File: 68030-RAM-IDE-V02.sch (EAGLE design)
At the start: 71 parts, among them IC1 REG1117, IC10 ICS570B, IC2 74HCT245PW, IC3 74AC16245, IC4 AM29F010S, IC5 74ALVT16543, IC6 74ALVT16543, IC7 XC95288XL-TQ144, IC8 K4S56163, IC9 K4S56163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

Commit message: burst still buggy :(
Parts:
- added C37, C38: 100pF, rcl:C-EUC0603K
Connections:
- net GND: now also C37.2, C38.2
- net LE_30_RAM: now also C38.1
- net LE_RAM_30: now also C37.1

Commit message: fooling around mit cl2
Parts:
- R10, R11: value (none) -> 33
- R12, R13: value (none) -> 4k7
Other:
- moved on the sheet: C36, IC10G$2, SJ1
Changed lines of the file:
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@@
 <part name="SJ1" library="jumper" deviceset="SJ2W" device=""/>
 <part name="C36" library="rcl" deviceset="C-EU" device="C0603K"/>
-<part name="R10" library="rcl" deviceset="R-EU_" device="R0603"/>
-<part name="R11" library="rcl" deviceset="R-EU_" device="R0603"/>
-<part name="R12" library="rcl" deviceset="R-EU_" device="R0603"/>
-<part name="R13" library="rcl" deviceset="R-EU_" device="R0603"/>
+<part name="R10" library="rcl" deviceset="R-EU_" device="R0603" value="33"/>
+<part name="R11" library="rcl" deviceset="R-EU_" device="R0603" value="33"/>
+<part name="R12" library="rcl" deviceset="R-EU_" device="R0603" value="4k7"/>
+<part name="R13" library="rcl" deviceset="R-EU_" device="R0603" value="4k7"/>
 <part name="SJ2" library="jumper" deviceset="SJ2W" device=""/>
 <part name="C37" library="rcl" deviceset="C-EU" device="C0603K" value="100pF"/>
@@
 <instance part="GND33" gate="1" x="66.04" y="5.08"/>
 <instance part="IC10" gate="G$1" x="200.66" y="142.24"/>
-<instance part="IC10" gate="G$2" x="215.9" y="116.84"/>
-<instance part="GND34" gate="1" x="215.9" y="104.14"/>
-<instance part="SJ1" gate="G$1" x="215.9" y="132.08" rot="R90"/>
-<instance part="C36" gate="G$1" x="226.06" y="119.38"/>
+<instance part="IC10" gate="G$2" x="215.9" y="109.22"/>
+<instance part="GND34" gate="1" x="215.9" y="96.52"/>
+<instance part="SJ1" gate="G$1" x="215.9" y="124.46" rot="R90"/>
+<instance part="C36" gate="G$1" x="226.06" y="111.76"/>
 <instance part="R10" gate="G$1" x="223.52" y="152.4"/>
 <instance part="R11" gate="G$1" x="223.52" y="149.86"/>
@@
 <pinref part="GND34" gate="1" pin="GND"/>
 <pinref part="IC10" gate="G$2" pin="GND"/>
-<wire x1="215.9" y1="106.68" x2="215.9" y2="109.22" width="0.1524" layer="91"/>
+<wire x1="215.9" y1="99.06" x2="215.9" y2="101.6" width="0.1524" layer="91"/>
 <pinref part="C36" gate="G$1" pin="2"/>
-<wire x1="215.9" y1="109.22" x2="226.06" y2="109.22" width="0.1524" layer="91"/>
-<wire x1="226.06" y1="109.22" x2="226.06" y2="114.3" width="0.1524" layer="91"/>
-<junction x="215.9" y="109.22"/>
+<wire x1="215.9" y1="101.6" x2="226.06" y2="101.6" width="0.1524" layer="91"/>
+<wire x1="226.06" y1="101.6" x2="226.06" y2="106.68" width="0.1524" layer="91"/>
+<junction x="215.9" y="101.6"/>
 </segment>
 <segment>
@@
 <segment>
 <pinref part="SJ1" gate="G$1" pin="1"/>
-<wire x1="210.82" y1="132.08" x2="208.28" y2="132.08" width="0.1524" layer="91"/>
+<wire x1="210.82" y1="124.46" x2="208.28" y2="124.46" width="0.1524" layer="91"/>
+<label x="208.28" y="124.46" size="1.778" layer="95" rot="R180"/>
 </segment>
 </net>
@@
 <pinref part="IC10" gate="G$1" pin="ICLK"/>
 <wire x1="187.96" y1="147.32" x2="172.72" y2="147.32" width="0.1524" layer="91"/>
+<label x="172.72" y="147.32" size="1.778" layer="95" rot="R180"/>
 </segment>
 </net>
@@
 <segment>
 <pinref part="C36" gate="G$1" pin="1"/>
-<wire x1="226.06" y1="121.92" x2="226.06" y2="127" width="0.1524" layer="91"/>
+<wire x1="226.06" y1="114.3" x2="226.06" y2="119.38" width="0.1524" layer="91"/>
 <pinref part="SJ1" gate="G$1" pin="2"/>
-<wire x1="226.06" y1="127" x2="215.9" y2="127" width="0.1524" layer="91"/>
+<wire x1="226.06" y1="119.38" x2="215.9" y2="119.38" width="0.1524" layer="91"/>
 <pinref part="IC10" gate="G$2" pin="VCC"/>
-<wire x1="215.9" y1="127" x2="215.9" y2="124.46" width="0.1524" layer="91"/>
-<junction x="215.9" y="127"/>
+<wire x1="215.9" y1="119.38" x2="215.9" y2="116.84" width="0.1524" layer="91"/>
+<junction x="215.9" y="119.38"/>
 </segment>
 </net>
@@
 <segment>
 <pinref part="SJ1" gate="G$1" pin="3"/>
-<wire x1="220.98" y1="132.08" x2="223.52" y2="132.08" width="0.1524" layer="91"/>
+<wire x1="220.98" y1="124.46" x2="223.52" y2="124.46" width="0.1524" layer="91"/>
+<label x="223.52" y="124.46" size="1.778" layer="95"/>
 </segment>
 <segment>
@@
 <pinref part="R12" gate="G$1" pin="2"/>
 <wire x1="185.42" y1="167.64" x2="185.42" y2="165.1" width="0.1524" layer="91"/>
+<label x="185.42" y="167.64" size="1.778" layer="95"/>
 </segment>
 </net>
@@
 <pinref part="SJ2" gate="G$1" pin="3"/>
 <wire x1="198.12" y1="129.54" x2="193.04" y2="129.54" width="0.1524" layer="91"/>
+<label x="205.74" y="137.16" size="1.778" layer="95"/>
 </segment>
 <segment>
@@
 <pinref part="SJ2" gate="G$1" pin="1"/>
 <wire x1="228.6" y1="139.7" x2="193.04" y2="139.7" width="0.1524" layer="91"/>
+<label x="205.74" y="139.7" size="1.778" layer="95"/>
 </segment>
 <segment>

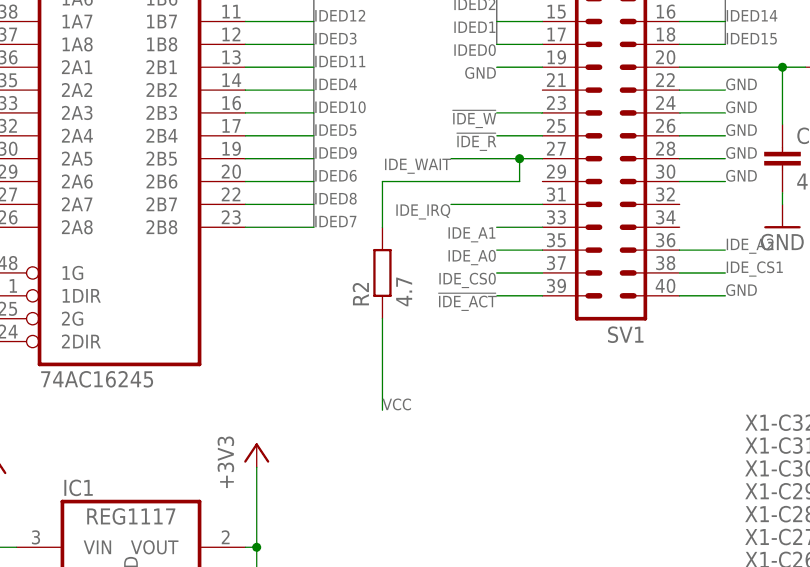
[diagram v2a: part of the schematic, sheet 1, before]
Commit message: Fixed some values in pcb and cleaned code
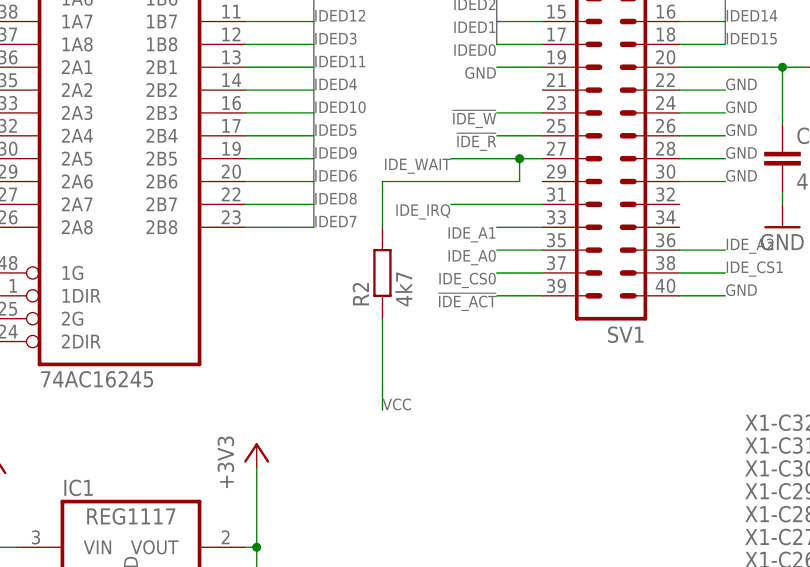
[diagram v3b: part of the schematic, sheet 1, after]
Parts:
- C36: value (none) -> 100nF
- R2: value 4.7 -> 4k7
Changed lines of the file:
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@@
 <part name="SV1" library="con-harting-ml" deviceset="ML40" device=""/>
 <part name="C2" library="rcl" deviceset="C-EU" device="C0805K" value="47µF"/>
-<part name="R2" library="rcl" deviceset="R-EU_" device="R0603" value="4.7"/>
+<part name="R2" library="rcl" deviceset="R-EU_" device="R0603" value="4k7"/>
 <part name="R3" library="rcl" deviceset="R-EU_" device="R2512" value="500mA"/>
 <part name="IC4" library="am29-memory" deviceset="AM29F010S" device=""/>
@@
 <part name="GND34" library="SUPPLY1" deviceset="GND" device=""/>
 <part name="SJ1" library="jumper" deviceset="SJ2W" device=""/>
-<part name="C36" library="rcl" deviceset="C-EU" device="C0603K"/>
+<part name="C36" library="rcl" deviceset="C-EU" device="C0603K" value="100nF"/>
 <part name="R10" library="rcl" deviceset="R-EU_" device="R0603" value="33"/>
 <part name="R11" library="rcl" deviceset="R-EU_" device="R0603" value="33"/>
